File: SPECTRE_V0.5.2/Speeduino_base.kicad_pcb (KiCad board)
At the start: 2 copper layers, 100 x 93 mm, 218 parts, among them J1 Conn_01x06_Male, J2 Conn_02x04_Odd_Even, J3 ProtoArea, Q1 AO3400, Q10 BSP78, Q11 BSP78, Q12 AO3400, Q13 BSP78, Q14 BSP78, Q15 BSP78, Q16 BSP78, Q17 BSP78, Q18 BSP78, Q19 BSP78, Q20 BSP78, Q21 BSP78, Q6 AO3400, Q7 AO3400, Q8 AO3400, Q9 AO3400, U1 MAX9926UAEE+, U2 LM78M05_TO220, U3 TL431DBZ, U4 molex_48pin, U5 TJA1050, U6 MAX3232, U7 MIC4427, U8 MIC4427, U9 MIC4427

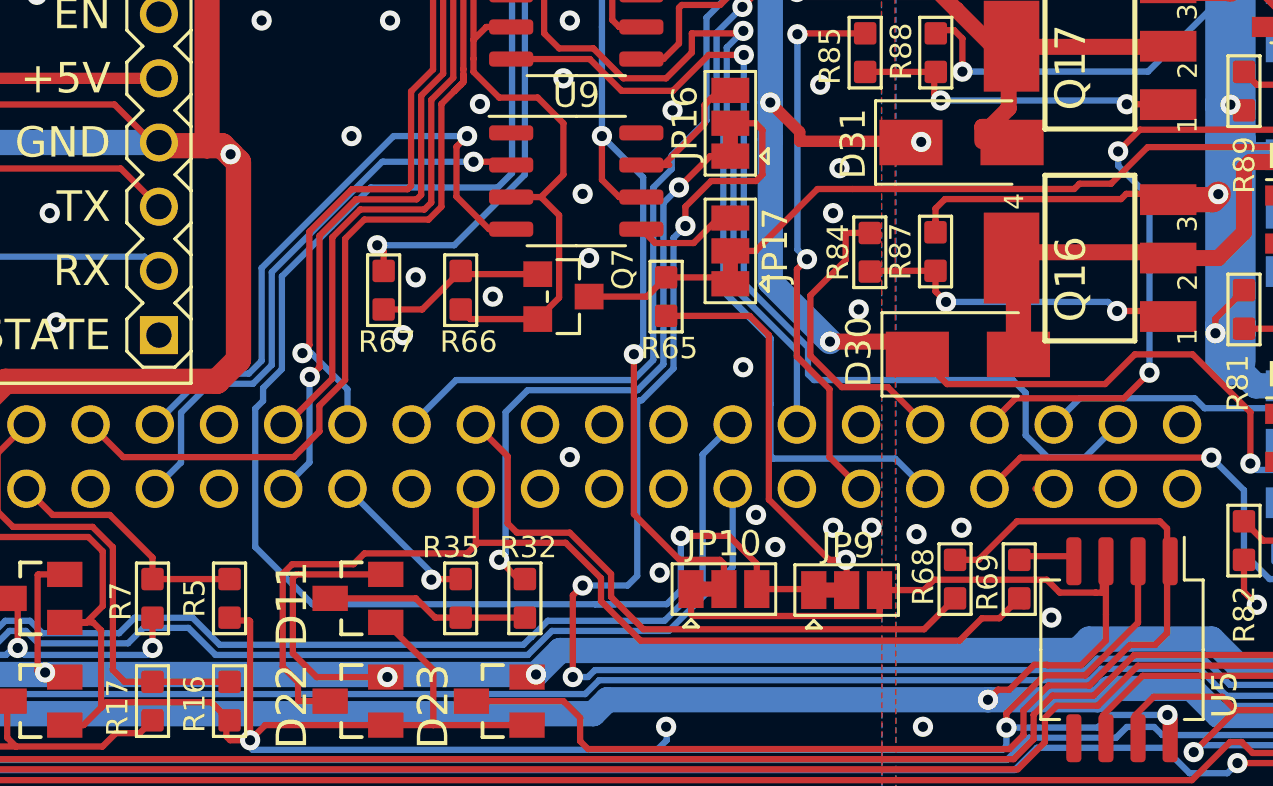
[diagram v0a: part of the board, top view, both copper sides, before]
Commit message: Update ign5 pin
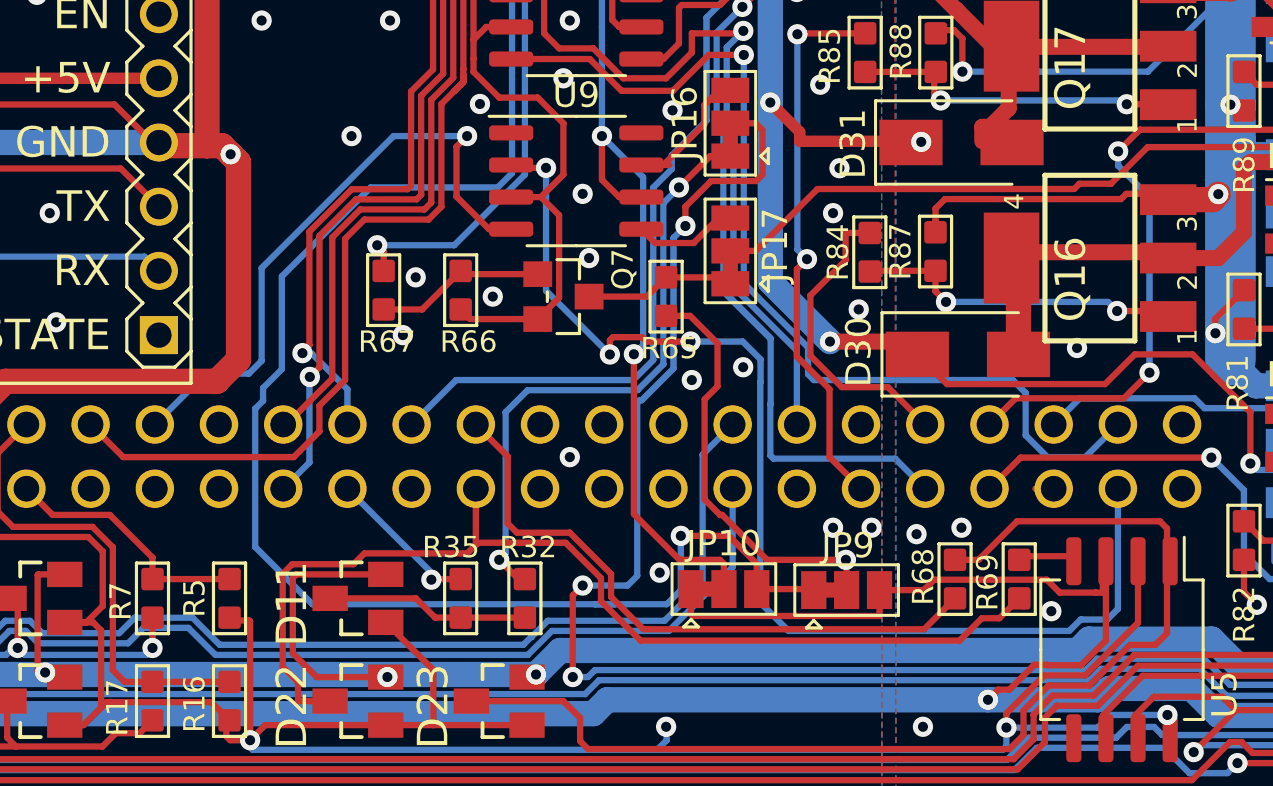
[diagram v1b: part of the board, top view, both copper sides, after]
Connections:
- U9 pad 2: PB6 -> PD9
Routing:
- net PD9: track 0.00 -> 46.8 mm, vias 0 -> 3
- net PB6: track 23.4 -> 0.00 mm, vias 1 -> 0
- net Net-(JP9-Pad2): track 16.4 -> 17.0 mm
- net PWR_GND: vias 94 -> 95
- net GND: vias 158 -> 157

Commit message: Updates on V0.5.2
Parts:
- removed D24, D25: 1N4007, Diode_SMD:D_SMA
- removed JP17: SolderJumper_3_Bridged12, Jumper:SolderJumper-3_P1.3mm_Bridged12_Pad1.0x1.5mm
- removed Q8, Q9: AO3400, Speeduino_base:SOT-23
- removed R70, R71: 100R, Speeduino_base:R0603
- removed R72, R73: 10k, Speeduino_base:R0603
- added JP18: SolderJumper_3_Bridged12, Jumper:SolderJumper-3_P1.3mm_Bridged12_Pad1.0x1.5mm, B.Cu at (211.3, 68.6)
- added U10: MIC4427, Package_SO:SO-8_3.9x4.9mm_P1.27mm, F.Cu at (192.8, 36.3)
- JP16: moved to B.Cu
- moved JP16 37.6 mm to (203.2, 85.3), turned to 180 degrees
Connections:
- JP16 pad 1: FLEX_FUEL_IN -> GND
- JP16 pad 3: IGN5-OUT -> IGN6-OUT
- U4 pad 22: GND -> Net-(JP18-Pad2)
- U4 pad 26: GND -> Net-(JP16-Pad2)
- U4 pad 38: Net-(JP16-Pad2) -> FLEX_FUEL_IN
- U4 pad 48: Net-(JP17-Pad2) -> TACHO-OUT
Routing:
- net IGN5-OUT: track 6.29 -> 102.9 mm, vias 0 -> 3
- net Net-(JP16-Pad2): track 110.5 -> 23.4 mm, vias 3 -> 0
- net FLEX_FUEL_IN: track 24.1 -> 86.9 mm, vias 2 -> 1
- net IGN6-OUT: track 4.16 -> 49.9 mm, vias 0 -> 3
- net TACHO-OUT: track 6.39 -> 47.2 mm
- net Net-(JP17-Pad2): track 38.7 -> 0.00 mm
- net VBAT: track 339.7 -> 306.6 mm
- net V_IDLE: track 5.19 -> 23.9 mm
- net Spare_2-Out: track 39.0 -> 25.4 mm, vias 4 -> 2
- net Net-(JP18-Pad2): track 0.00 -> 10.8 mm, vias 0 -> 1
- net GND: track 696.6 -> 706.9 mm, vias 157 -> 158
- net PWR_GND: track 464.9 -> 455.5 mm, vias 95 -> 98
- net PB13: track 13.6 -> 20.2 mm, vias 1 -> 2
- net Net-(Q9-Pad1): track 5.51 -> 0.00 mm
- net PB12: track 12.9 -> 18.2 mm, vias 1 -> 2
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
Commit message: Update zener value
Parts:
- D33, D35, D36, D39, D40, D43, D44, D45: value D_Schottky_Small -> 1N4148WS
- D34, D37, D38, D41, D42, D46, D47, D48: value BZX84C56 -> BZX84C39
